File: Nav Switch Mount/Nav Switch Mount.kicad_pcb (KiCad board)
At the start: 2 copper layers, 23.1 x 12.8 mm, 9 parts, among them J1 Conn_01x06, U1 SKQUAAA010

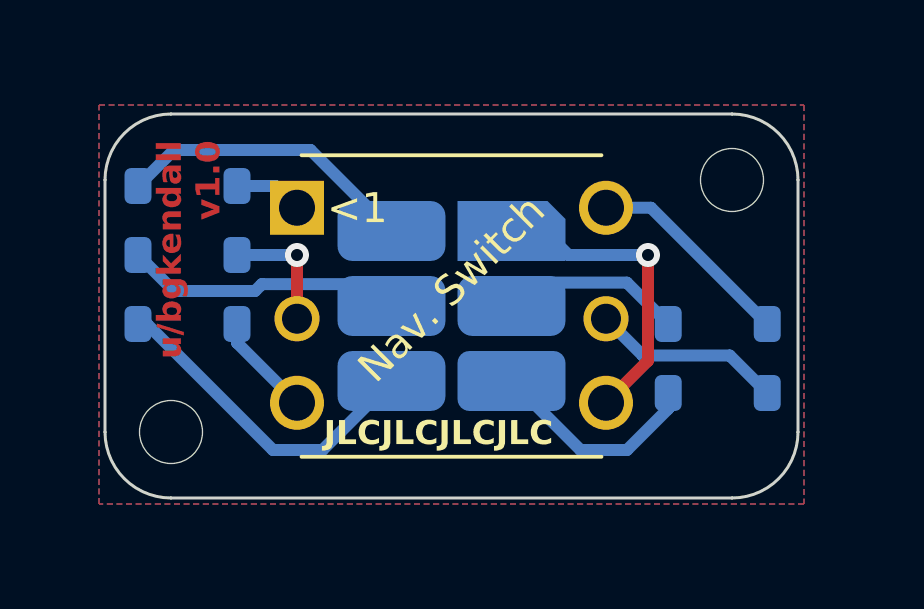
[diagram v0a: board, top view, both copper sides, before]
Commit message: Scoot D4 and D5 to the left to be same distance from switch as D1–3
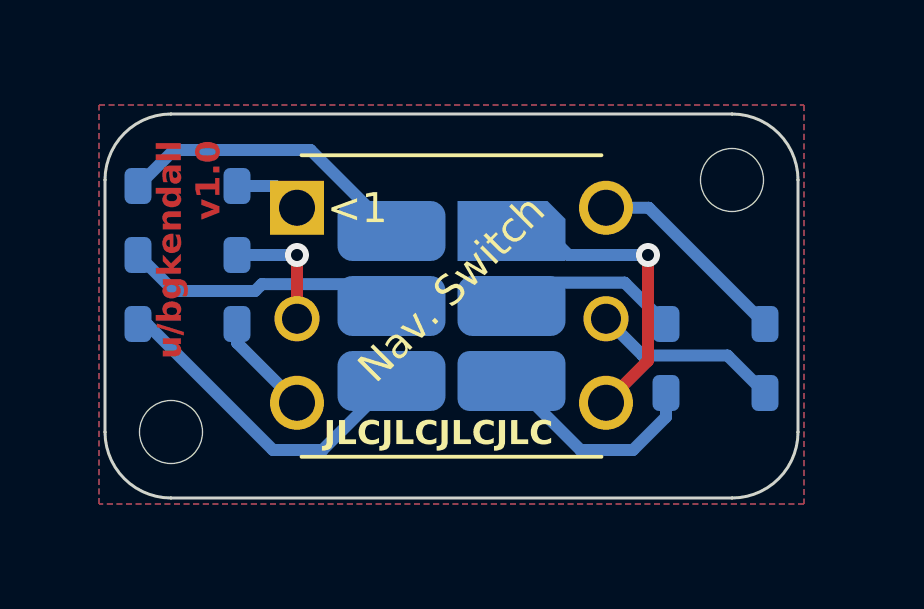
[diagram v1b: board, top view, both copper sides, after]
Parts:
- moved D4 0.08 mm to (167.8, 54.9)
- moved D5 0.08 mm to (167.8, 52.6)
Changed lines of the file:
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@@
       (plot_on_all_layers_selection 0x0000000_00000000)
       (disableapertmacros false)
-      (usegerberextensions false)
-      (usegerberattributes true)
-      (usegerberadvancedattributes true)
-      (creategerberjobfile true)
+      (usegerberextensions true)
+      (usegerberattributes false)
+      (usegerberadvancedattributes false)
+      (creategerberjobfile false)
       (dashed_line_dash_ratio 12.000000)
       (dashed_line_gap_ratio 3.000000)
@@
       (psa4output false)
       (plotreference true)
-      (plotvalue true)
+      (plotvalue false)
       (plotinvisibletext false)
       (sketchpadsonfab false)
-      (subtractmaskfromsilk false)
+      (subtractmaskfromsilk true)
       (outputformat 1)
       (mirror false)
-      (drillshape 1)
+      (drillshape 0)
       (scaleselection 1)
-      (outputdirectory "")
+      (outputdirectory "./Gerbers")
     )
   )
@@
   )
   (footprint "Diode_SMD:D_SOD-123" (layer "B.Cu")
-    (at 167.925 52.6 180)
+    (at 167.85 52.6 180)
     (descr "SOD-123")
     (tags "SOD-123")
@@
   )
   (footprint "Diode_SMD:D_SOD-123" (layer "B.Cu")
-    (at 167.925 54.9 180)
+    (at 167.85 54.9 180)
     (descr "SOD-123")
     (tags "SOD-123")
@@
   (segment (start 154.75 56.8) (end 157.05 54.5) (width 0.4) (layer "B.Cu") (net 6))
   (segment (start 148.6 52.6) (end 148.9 52.6) (width 0.4) (layer "B.Cu") (net 6))
-  (segment (start 168.325 53.65) (end 169.575 54.9) (width 0.4) (layer "B.Cu") (net 7))
+  (segment (start 168.25 53.65) (end 169.5 54.9) (width 0.4) (layer "B.Cu") (net 7))
   (segment (start 164.2 52.425) (end 165.425 53.65) (width 0.4) (layer "B.Cu") (net 7))
-  (segment (start 165.425 53.65) (end 168.325 53.65) (width 0.4) (layer "B.Cu") (net 7))
-  (segment (start 164.9 56.8) (end 166.275 55.425) (width 0.4) (layer "B.Cu") (net 8))
-  (segment (start 163.35 56.8) (end 164.9 56.8) (width 0.4) (layer "B.Cu") (net 8))
-  (segment (start 166.275 55.425) (end 166.275 54.9) (width 0.4) (layer "B.Cu") (net 8))
+  (segment (start 165.425 53.65) (end 168.25 53.65) (width 0.4) (layer "B.Cu") (net 7))
+  (segment (start 163.35 56.8) (end 165.1 56.8) (width 0.4) (layer "B.Cu") (net 8))
+  (segment (start 166.2 55.7) (end 166.2 54.9) (width 0.4) (layer "B.Cu") (net 8))
   (segment (start 161.05 54.5) (end 163.35 56.8) (width 0.4) (layer "B.Cu") (net 8))
-  (segment (start 164.2 48.725) (end 165.7 48.725) (width 0.4) (layer "B.Cu") (net 9))
-  (segment (start 165.7 48.725) (end 169.575 52.6) (width 0.4) (layer "B.Cu") (net 9))
-  (segment (start 161.829 51.221) (end 164.896 51.221) (width 0.4) (layer "B.Cu") (net 10))
-  (segment (start 164.896 51.221) (end 166.275 52.6) (width 0.4) (layer "B.Cu") (net 10))
+  (segment (start 165.1 56.8) (end 166.2 55.7) (width 0.4) (layer "B.Cu") (net 8))
+  (segment (start 164.2 48.725) (end 165.625 48.725) (width 0.4) (layer "B.Cu") (net 9))
+  (segment (start 165.625 48.725) (end 169.5 52.6) (width 0.4) (layer "B.Cu") (net 9))
+  (segment (start 164.821 51.221) (end 166.2 52.6) (width 0.4) (layer "B.Cu") (net 10))
+  (segment (start 161.829 51.221) (end 164.821 51.221) (width 0.4) (layer "B.Cu") (net 10))
   (segment (start 165.6 50.3) (end 165.6 53.825) (width 0.4) (layer "F.Cu") (net 12))
   (segment (start 165.6 53.825) (end 164.2 55.225) (width 0.4) (layer "F.Cu") (net 12))

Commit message: Move footprints to project library
Also:

 * Redesigned diode footprint with more compact labelling.
 * Redesigned switch footprint to centre on middle of switch and added 3D model.
 * Removed 3D model from header footprint.
 * Narrowed and widened PCB.
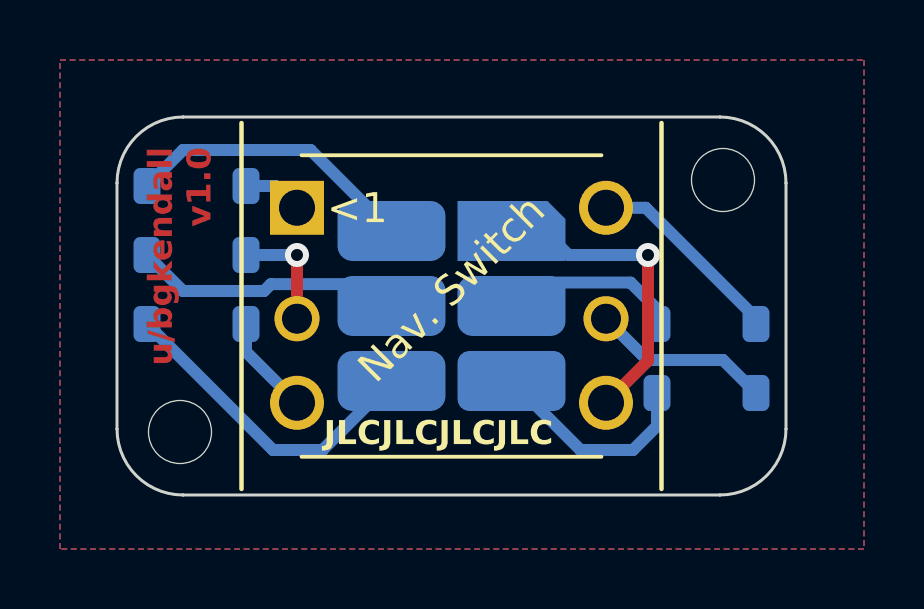
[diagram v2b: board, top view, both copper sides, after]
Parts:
- D1, D2, D3, D4, D5: footprint Diode_SMD:D_SOD-123 -> _Project_Library:D_SOD-123
- J1: footprint Connector_PinHeader_1.00mm:PinHeader_1x06_P1.00mm_Vertical_SMD_Pin1Right -> _Project_Library:Header_2x3
- U1: footprint SKQUAAA010:SKQUAAA010 -> _Project_Library:Nav_Switch_SKQUAAA010
- moved U1 6.08 mm to (159.1, 52.0)
- moved D1 0.30 mm to (150.6, 48.0)
- moved D2 0.30 mm to (150.6, 50.3)
- moved D3 0.30 mm to (150.6, 52.6)
- moved H1 0.30 mm to (150.0, 56.2)
- moved H2 0.30 mm to (168.1, 47.8)
- moved D4 0.30 mm to (167.6, 54.9)
- moved D5 0.30 mm to (167.6, 52.6)
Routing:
- added copper zone on B.Cu, net (none)
- added copper zone on F.Cu, net (none)
- removed copper zone on B.Cu, net GND
- removed copper zone on F.Cu, net GND
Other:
- board size 23.1 x 12.8 mm -> 22.3 x 12.6 mm
